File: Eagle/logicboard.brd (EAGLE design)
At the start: 101.3 x 54.6 mm, 28 parts, among them U2 ENC28J60-SO, U3 ATMEGA328P_PDIP, Y2 25MHz, Y3 16MHz

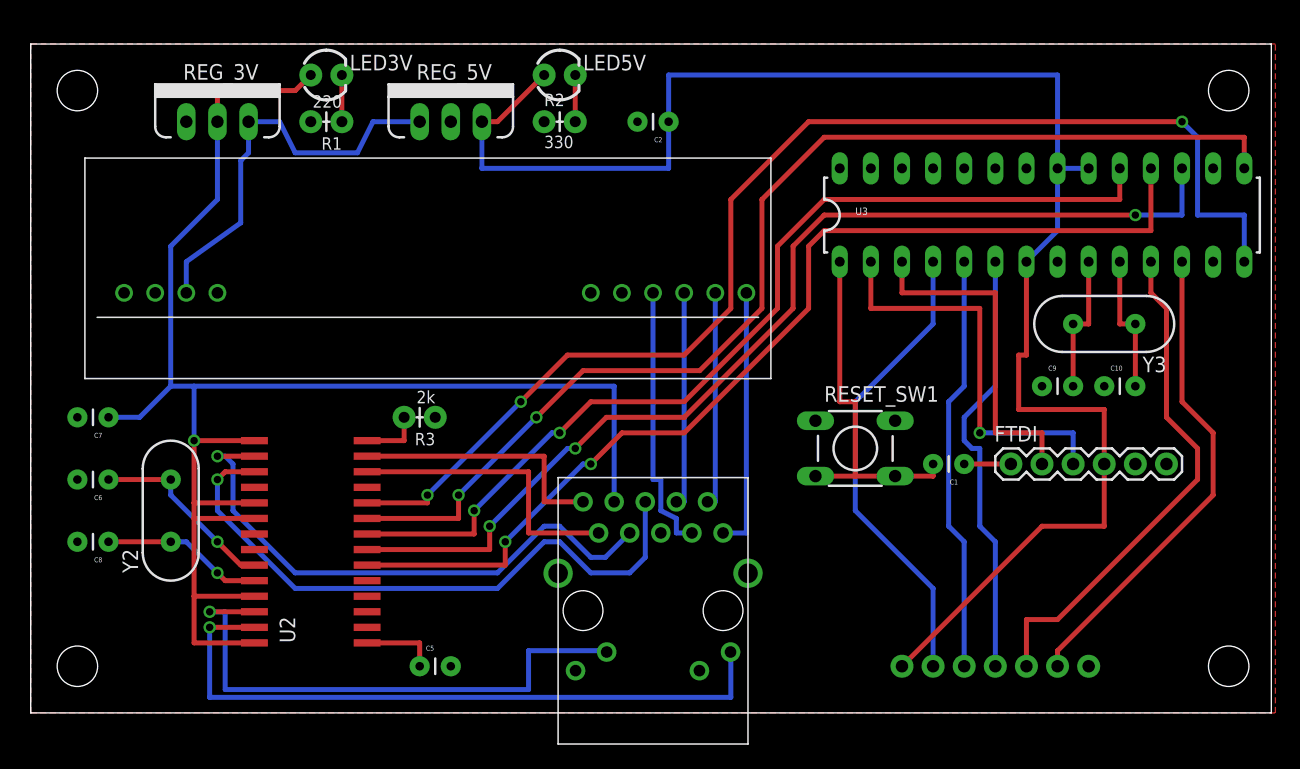
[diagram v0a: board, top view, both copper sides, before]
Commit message: Update schematic to include on-board 200V psu
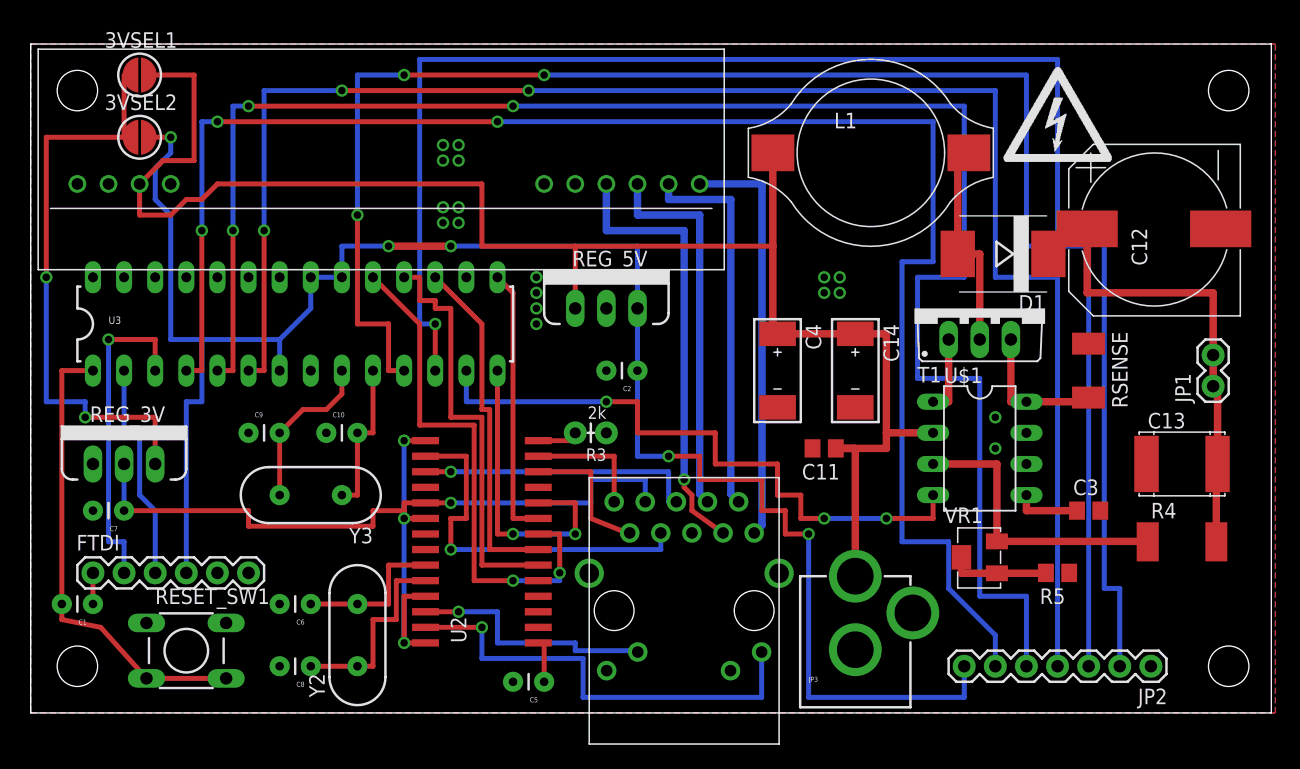
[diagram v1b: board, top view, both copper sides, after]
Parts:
- removed LED3V, LED5V: (no value), SparkFun-LED:LED3MM
- removed R1: 220, SparkFun-Resistors:AXIAL-0.1
- removed R2: 330, SparkFun-Resistors:AXIAL-0.1
- added 3VSEL1: JACK, SparkFun-Passives:PAD-JUMPER-2-NO_YES_SILK_ROUND
- added 3VSEL2: 5V, SparkFun-Passives:PAD-JUMPER-2-NO_YES_SILK_ROUND
- added C11, C3: 100n, rcl:C0805
- added C12: 4u7,250V, nick:NICHICON-UJ-12
- added C13: 100n,250V, nick:C2420
- added C14: 10uF,25V, nick:C-EIA-7343
- added C4: 100uF,35V, nick:C-EIA-7343
- added D1: ES2F, diode:SMC
- added JP1: M02PTH, SparkFun-Connectors:1X02
- added JP3: POWER_JACKPTH, SparkFun-Connectors:POWER_JACK_PTH
- added L1: 100uH, nick:L-B82479
- added R4: 1M5, rcl:R2512
- added R5: 10K, rcl:R0805
- added RSENSE: 0R050, rcl:R2010
- added T1: IRF644PBF, transistor-power:TO220BV
- added U$1: MAX1771, max1771:8-DIP
- added U$4: HIGHVOLTAGE, highvoltage:HIGHVOLTAGE
- added VR1: 5K, nick:BOURNS-3214W
- JP2: value BUS -> (none)
- moved FTDI 75.5 mm to (5.08, 11.4)
- moved C1 72.0 mm to (5.08, 8.89)
- moved Y3 66.3 mm to (22.9, 17.8)
- moved C9 64.9 mm to (17.8, 22.9)
- moved C10 63.6 mm to (24.1, 22.9)
- moved U3 61.6 mm to (21.6, 31.8)
- moved RESET_SW1 57.1 mm to (12.7, 5.08)
- moved REG_3V 29.0 mm to (7.62, 20.3)
- moved C2 20.5 mm to (49.5, 27.9)
- moved REG_5V 19.8 mm to (47.0, 33.0)
- moved C6 19.4 mm to (22.9, 8.89)
- moved C8 19.4 mm to (22.9, 3.81)
- moved Y2 18.3 mm to (26.7, 6.35)
- moved R3 14.0 mm to (47.0, 22.9)
- moved U2 14.0 mm to (36.8, 14.0)
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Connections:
- removed net N$2: LED5V.K, R2.P$2
- removed net POE_IN: REG_3V.3, REG_5V.1, U$2.P$8
- new net 12V: 3VSEL1.2, C11.1, C14.+, C4.+, JP3.PWR, L1.P$1, REG_5V.1, U$1.V+, U$2.P$8
- new net EXT: T1.G, U$1.EXT
- new net HV_VCC: C12.2, C13.P$1, D1.C, JP1.1, JP1.2, R4.2
- new net N$10: C3.1, U$1.REF
- new net N$15: D1.A, L1.P$2, T1.D
- new net N$7: R5.2, VR1.1, VR1.2
- new net N$8: R4.1, U$1.FB, VR1.3
- new net N$9: RSENSE.2, T1.S, U$1.CS
- new net SHDN: U$1.SHDN, U3.13
- net 3.3V: no longer LED3V.A
- net 5V: now also 3VSEL2.2; no longer LED5V.A
- net GND: now also C11.2, C12.1, C13.P$2, C14.-, C3.2, C4.-, JP3.GND, JP3.GNDBREAK, R5.1, RSENSE.1, U$1.AGND, U$1.GND; no longer R1.P$2, R2.P$1
- net N$1: now also 3VSEL1.1, 3VSEL2.1, REG_3V.3; no longer LED3V.K, R1.P$1
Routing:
- net 12V: track 0.00 -> 134.2 mm
- net N_SCK: track 34.1 -> 141.0 mm, vias 0 -> 3
- net N_SCL: track 35.5 -> 135.9 mm, vias 0 -> 3
- net N_SER: track 38.3 -> 133.7 mm, vias 0 -> 3
- net N_G: track 39.3 -> 133.4 mm, vias 0 -> 1
- net N_RCK: track 41.9 -> 135.9 mm, vias 0 -> 3
- net E_RESET: track 100.8 -> 25.2 mm, vias 3 -> 2
- net E_CS: track 93.4 -> 22.3 mm, vias 2 -> 0
- net MOSI: track 85.7 -> 28.4 mm, vias 3 -> 0
- net SHDN: track 0.00 -> 52.1 mm, vias 0 -> 3
- net MISO: track 84.5 -> 34.4 mm, vias 2 -> 0
- net 3.3V: track 131.2 -> 81.2 mm, vias 1 -> 4
- net N$1: track 3.81 -> 47.0 mm, vias 0 -> 2
- net HV_VCC: track 0.00 -> 40.3 mm
- net SCK: track 79.4 -> 43.3 mm
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- added copper zone on layer 16, net GND

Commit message: Ensure latest eagle
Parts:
- added G1: CR2032V, battery:CR2032V
- added Q1: (no value), crystal:TC26V
- added U$5: PT7C4302, Custom:SO8
- moved C7 16.7 mm to (24.1, 14.0), turned to 270 degrees
- moved REG_3V 8.98 mm to (14.0, 14.0)
- moved C2 4.26 mm to (51.4, 31.8), turned to 90 degrees
- moved C1 3.59 mm to (7.62, 6.35), turned to 270 degrees
- moved FTDI 2.84 mm to (7.62, 10.2)
- moved REG_5V 1.27 mm to (45.7, 33.0)
- moved RESET_SW1 1.27 mm to (14.0, 5.08)
- moved C6 1.27 mm to (22.9, 7.62)
- moved Y3 1.27 mm to (24.1, 17.8)
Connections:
- removed net N_G: JP2.2, U3.12
- removed net N_SCL: JP2.4, U3.6
- new net N$11: Q1.2, U$5.2
- new net N$12: Q1.1, U$5.3
- new net N$2: G1.+, U$5.8
- new net RTC_CLK: U$5.7, U3.6
- new net RTC_IO: U$5.6, U3.12
- new net RTC_RST: U$5.5, U3.16
- net 5V: now also JP2.4, U$5.1
- net GND: now also G1.-, JP2.2, U$5.4
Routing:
- net N_SCL: track 135.9 -> 0.00 mm, vias 3 -> 0
- net N_G: track 133.4 -> 0.00 mm, vias 1 -> 0
- net GND: track 0.00 -> 129.5 mm, vias 18 -> 19
- net 5V: track 152.0 -> 280.5 mm, vias 5 -> 9
- net RTC_RST: track 0.00 -> 36.1 mm, vias 0 -> 1
- net 3.3V: track 81.2 -> 54.5 mm
- net RESET: track 38.2 -> 11.9 mm
- net RTC_IO: track 0.00 -> 24.7 mm, vias 0 -> 1
- net RTC_CLK: track 0.00 -> 8.20 mm
- net N$20: track 13.4 -> 8.30 mm
- net FTDI_TX: track 18.3 -> 22.9 mm
- net N$12: track 0.00 -> 4.38 mm
- net FTDI_RX: track 26.7 -> 30.5 mm
- net N$11: track 0.00 -> 3.12 mm
- net N$21: track 12.7 -> 11.4 mm
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
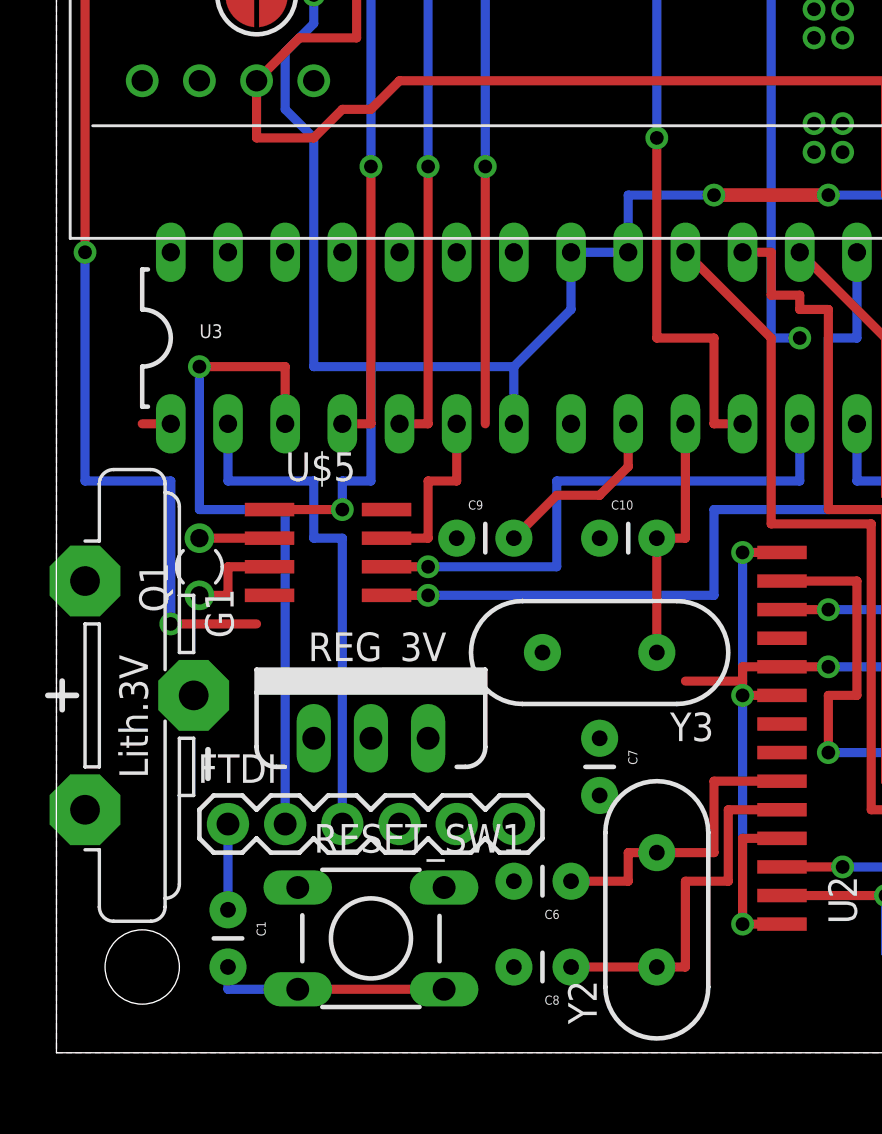
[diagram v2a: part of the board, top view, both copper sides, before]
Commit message: Update schematics, finish RTC addition
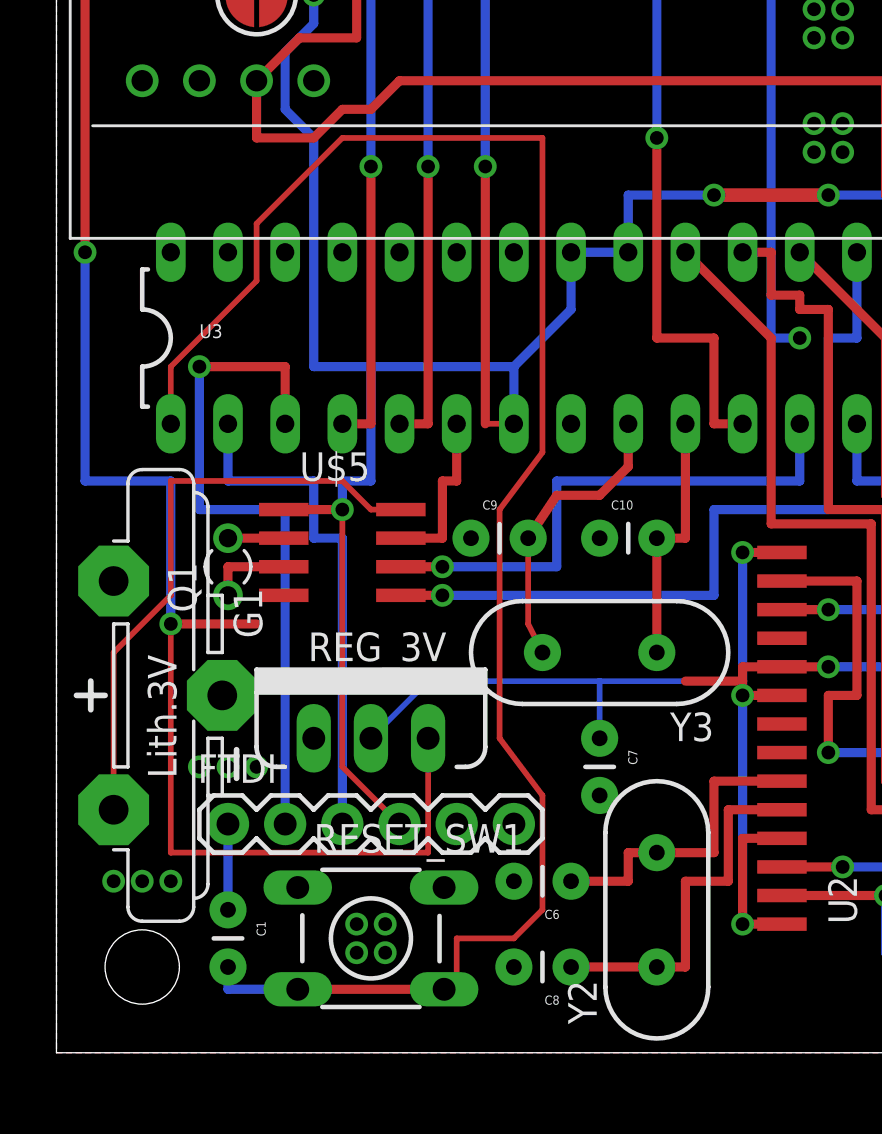
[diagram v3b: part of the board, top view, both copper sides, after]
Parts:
- moved Q1 1.27 mm to (7.62, 21.6)
- moved G1 1.27 mm to (5.08, 15.9)
- moved U$5 0.63 mm to (10.8, 25.4)
- moved C9 0.63 mm to (18.4, 22.9)
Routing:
- net RESET: track 11.9 -> 78.4 mm
- net N$1: track 47.0 -> 73.7 mm
- net N$2: track 0.00 -> 26.4 mm
- net 3.3V: track 54.5 -> 74.6 mm
- net 5V: track 280.5 -> 296.1 mm
- net N$20: track 8.30 -> 13.1 mm
- net RTC_RST: track 36.1 -> 35.5 mm
- net RTC_IO: track 24.7 -> 24.1 mm
- net RTC_CLK: track 8.20 -> 7.56 mm
- net N$12: track 4.38 -> 3.75 mm
- net N$11: track 3.12 -> 2.48 mm
- net GND: vias 19 -> 29
